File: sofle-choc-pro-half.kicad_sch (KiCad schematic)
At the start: 194 parts, among them J1 Connector, USB-TYPE-C-16P, J2 Connector, USB-TYPE-C-16P, J3 OLED 128x32, SW1 BOOT, SW10 F0, SW11 F1, SW12 F2, SW13 F3, SW14 F4, SW15 F5, SW16 F6 Choc/EC11, SW2 RESET, SW20 N0, SW21 N1, SW22 N2, SW23 N3, SW24 N4, SW25 N5, SW30 T0, SW31 T1, SW32 T2, SW33 T3, SW34 T4, SW35 T5, SW40 H0, SW41 H1, SW42 H2, SW43 H3, SW44 H4, SW45 H5, SW50 B0, SW51 B1, SW52 B2, SW53 B3, SW54 B4, SW55 B5, SW60 TH0, SW61 TH1, SW62 TH2, SW63 TH3, SW64 TH4, SW65 TH5 Choc/EC11, U1 RP2040, U2 USBLC6-2P6, U3 W25Q128JVPIQ, U4 USBLC6-2P6, U5 AP2112K-3.3, U6 SN74LV1T34DBVR, X1 ABM8-272-T3

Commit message: feat(pcb): put both halves in one project and one board
Both halves now live in one KiCad project: the schematic is one half sheet
used twice, as sheets Left and Right, and one board carries both halves
10 mm apart, so they are seen, checked and ordered together. Nothing moved
or was rewired: every pad sits where it did on the two old boards and every
pad net matches the new schematic.

- Edit sofle-choc-pro-half.kicad_sch once and both halves follow; Right
  references are the Left ones + 200
- Every net is per half, power included, through local power symbols, so
  the two halves can never join into one net
- One Ergogen run builds both halves, and the USB-C notches, case ports,
  spacer pockets and display openings hang off J1-J3 points, so board and
  case cannot drift apart
- Placement, LED snapping and hole placement work on both halves by
  (half, role)

Under the hood:
- sch: global labels made local; VBUS_FUSED names the F1-D1 net, which
  only had an auto name; H1-H5 are MountingHole symbols now
- pcb: right board brought in +139 mm with fresh UUIDs; its 29 unplaced
  support parts parked below it; pours clipped at the midline; J1/J2
  origins moved onto the board edge; the right HOST/LINK labels mirrored
  from the left, since they were stale copies at the left's coordinates
- rules: net class patterns and pair rules use sheet-prefixed names, which
  bare names never match; one skew rule per half so the pairs are not
  compared across halves
- ergogen: make_right.js becomes make_both.js; mounts.json replaces
  screws.json
- scripts: halves.py added; place_mounting_holes.py folded into
  place_from_ergogen.py; strip_signals.py keeps VBUS_FUSED as power
- fixes: the holes and J1/J2 had bare footprint ids or no sheet fields

ERC 0, parity 0, 452 unconnected (194 + 258, unrouted). DRC errors are the
26 known hole courtyard overlaps, 13 per half.
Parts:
- added H1, H2, H3, H4, H5: MountingHole, MountingHole:MountingHole_2.2mm_M2, symbol Mechanical:MountingHole
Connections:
- net VBUS_FUSED: now reaches D1.2, F1.2
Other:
- note added: "MOUNTING HOLES (placed from ergogen screw points)"

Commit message: feat(pcb): add a vbus tvs to both halves and move r210's via off its pad
Raw VBUS at each USB-C port now has surge protection ahead of the fuse,
and the right half's VBUS sense via no longer sits in a pad.

- D2/D202: SMF5.0A (LCSC C19077497, SOD-123FL) from VBUS to GND in the
  half sheet, on B.Cu beside J1/J201 with a 0.5 mm stub to the VBUS via
- D202 sits 1 mm east of the tightest spot so the B pour still feeds
  the right J1 GND patch (closer, the patch became isolated copper)
- The USB-C HOST labels move 2.7 mm down, clear of the new diodes
- R210's VBUS via moves beside pad 1 (it was centred in it and
  untented), fed on F.Cu past F201's VBUS_FUSED via

Verified: ERC 0 errors (27 warnings, unchanged); DRC 26
courtyards_overlap, 0 unconnected, 0 parity at all severities; GND
connected on both halves; jumper pad groups intact.
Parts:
- added D2: SMF5.0A, PCM_JLCPCB:D_SOD-123FL, symbol PCM_JLCPCB-Diodes:TVS-Uni,SMF5.0A
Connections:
- net GND: now also D2.2
- net VBUS: now also D2.1

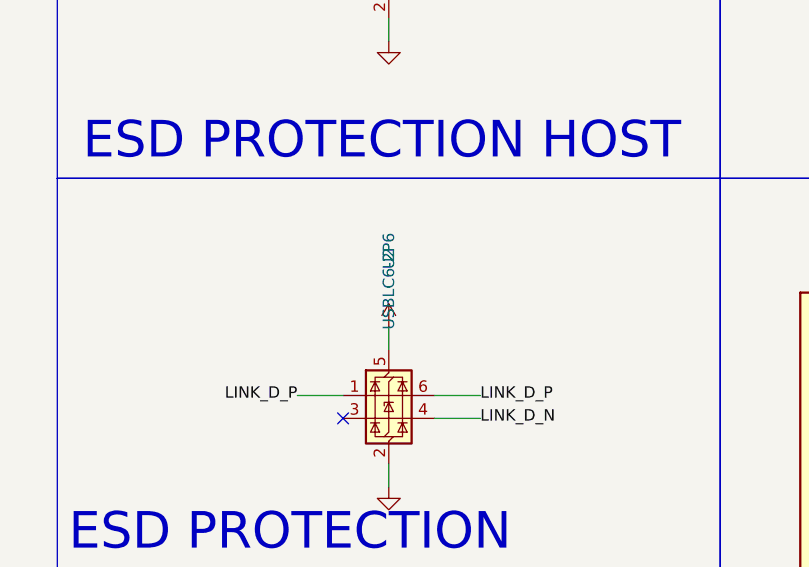
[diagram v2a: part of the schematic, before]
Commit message: fix(sch): give the 12 mhz crystal its own abm8-272-t3 symbol
X1/X201 borrowed the JLCPCB library's 20 pF crystal symbol (a different
part, C9002), so reviews flagged a 20 pF crystal on 15 pF load caps.

- New my-soffle:ABM8-272-T3_C20625731 symbol: same graphic and
  footprint, fields from the Abracon datasheet (10 pF load, C20625731)
- Frequency stability and 25 C tolerance corrected to +/-30 ppm (were
  the borrowed part's +/-20 and +/-10 ppm), on the board copies too
- Blank stock/price fields dropped from the new symbol

Verified: ERC 0 errors (27 warnings, unchanged); DRC 26
courtyards_overlap, 0 unconnected, 0 parity at all severities.
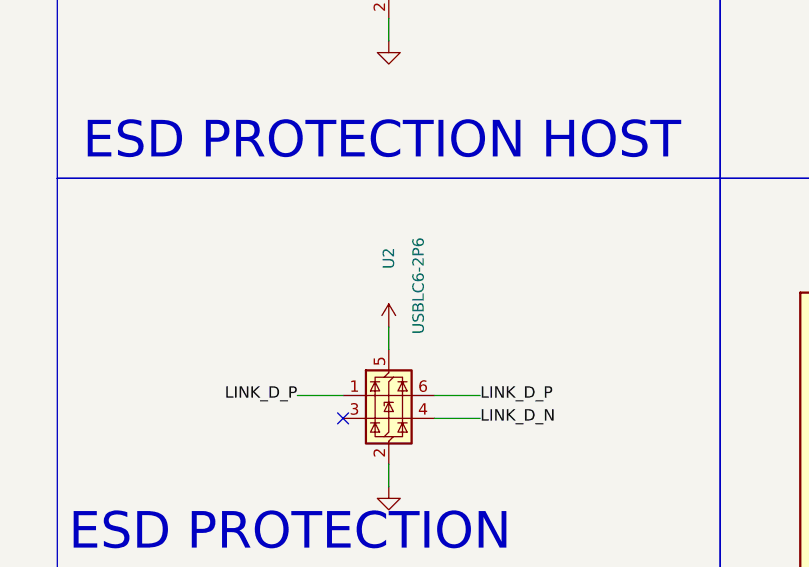
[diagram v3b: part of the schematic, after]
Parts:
- X1: symbol PCM_JLCPCB-Crystals:Crystal, 12MHz, 20pF -> my-soffle:ABM8-272-T3_C20625731; Frequency Stability ±20ppm -> ±30ppm; Normal Temperature Frequency Tolerance ±10ppm -> ±30ppm

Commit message: build(lib): vendor the used jlcpcb parts so the project opens anywhere
A clean clone now opens with every symbol, footprint and 3D model in
place: no Plugin and Content Manager package or KICAD8_3RD_PARTY path
is needed. Without the library, a reviewer saw 244 ERC and 286 DRC
items (missing symbols and footprints) and 292 missing 3D models.

- lib/jlcpcb/: the 16 symbols, 8 footprints and 8 models the design
  uses, from CDFER/JLCPCB-Kicad-Library (MIT, LICENSE included)
- The Choc hotswap model (kiswitch) moves into lib/my-soffle.3dshapes
- sym-lib-table/fp-lib-table keep their nicknames with ${KIPRJMOD}
  paths; the unused Crystals and Diode-Packages entries are dropped
- R7/R8 (27 ohm, C25100) get their own my-soffle:0402_27R_C25100
  symbol instead of the library's 33 ohm one
- README says what to install for each task; rule file notes the
  vendored copy

Verified with KICAD8_3RD_PARTY pointing at an empty folder and without:
both give ERC 0 errors (27 warnings) and DRC 26 courtyards_overlap,
0 unconnected, 0 parity at all severities; every board model resolves.
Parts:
- R7, R8: symbol PCM_JLCPCB-Resistors:0402,33Ω -> my-soffle:0402_27R_C25100
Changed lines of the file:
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@@
 	)
 	(symbol
-		(lib_id "PCM_JLCPCB-Resistors:0402,33Ω")
+		(lib_id "my-soffle:0402_27R_C25100")
 		(at 140.97 91.44 180)
 		(unit 1)
@@
 			)
 		)
-		(property "Description" ""
+		(property "Description" "27Ω ±1% 62.5mW 0402 thick film resistor (USB series termination)"
 			(at 140.97 91.44 0)
 			(hide yes)
@@
 	)
 	(symbol
-		(lib_id "PCM_JLCPCB-Resistors:0402,33Ω")
+		(lib_id "my-soffle:0402_27R_C25100")
 		(at 143.51 91.44 180)
 		(unit 1)
@@
 			)
 		)
-		(property "Description" ""
+		(property "Description" "27Ω ±1% 62.5mW 0402 thick film resistor (USB series termination)"
 			(at 143.51 91.44 0)
 			(hide yes)

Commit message: fix(pcb): place the usb-c connectors on jlc's footprint origin
The four USB-C receptacles were told to sit 2.55 mm from where their
pads are, so an assembled board would have had every host and link
connector misplaced. The offset that positions them was measured for
the old connector and never revisited when the board moved to the
mid-mount part.

- J1, J2, J201 and J202 now land on the pad field, matching JLC's own
  footprint for C19274022 to within 0.07 mm
- FT Position Offset goes from 0,1.394 to 0,3.945, the distance from
  our footprint's anchor at the connector mouth to that pad field
- README and the KiCad rules record why the Fabrication Toolkit runs
  with automatic translation off, and that a part swap invalidates a
  part's offset

Derived by fitting JLC's own footprints onto ours, the method that
reproduces the three offsets already on the board (270 on the SOT-563
and WSON-8, 180 on the stock SOT-23-5). ERC 0 errors; DRC 42 known
items, 0 unconnected, 0 parity.
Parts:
- J1, J2: FT Position Offset 0,1.394 -> 0,3.945
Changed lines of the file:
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@@
 			)
 		)
-		(property "FT Position Offset" "0,1.394"
+		(property "FT Position Offset" "0,3.945"
 			(at 29.21 39.37 0)
 			(hide yes)
@@
 			)
 		)
-		(property "FT Position Offset" "0,1.394"
+		(property "FT Position Offset" "0,3.945"
 			(at 109.22 271.78 0)
 			(hide yes)

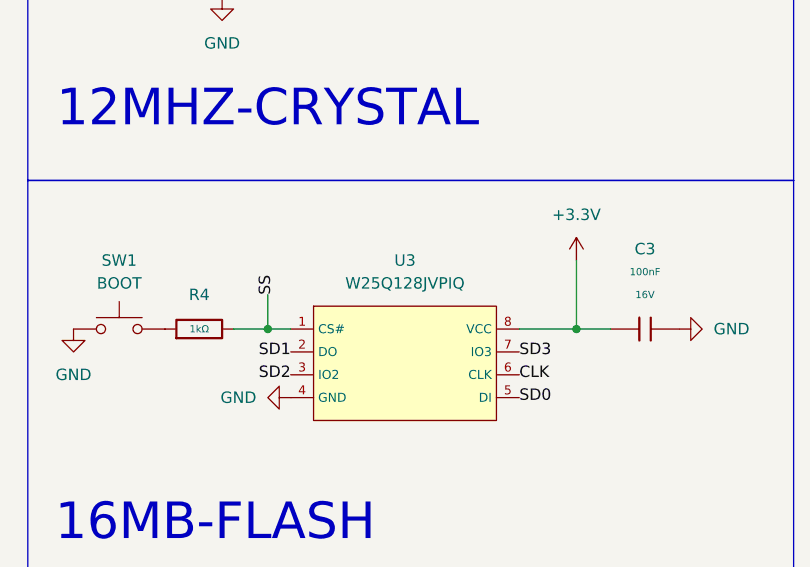
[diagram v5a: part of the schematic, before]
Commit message: feat(sch): swap the flash to the zetta zd25q128c
The Winbond W25Q128JVPIQ had climbed to EUR 2.74 each and fallen to
385 in stock at JLCPCB, making it both the most expensive line on the
board and the one most likely to be unavailable at order time. The
Zetta part is the same 128 Mbit in the same package for a third of the
money, so capacity is unchanged.

- EUR 27.39 to EUR 8.47 for the ten pieces a 5 board run needs, and
  2193 in stock instead of 385
- No copper changes: pin for pin identical (1 CS#, 2 SO/IO1, 3 WP#/IO2,
  4 VSS, 5 SI/IO0, 6 SCLK, 7 HOLD#/IO3, 8 VCC) on the same WSON-8 6x5
  land, verified against the part's own datasheet table 1 and against
  the RP2040 QSPI pins in its table 616
- FT Rotation Offset drops from 270 to 0, because JLC's drawing for
  this part sits 90 degrees from the Winbond one; U3 now writes 0 and
  U203 writes 90 into the placement file
- datasheets/ tracks the new part and drops the superseded one, and
  picks up the SMF5.0A sheet that was missing

ERC 0 errors; DRC 42 known items, 0 unconnected, 0 parity.
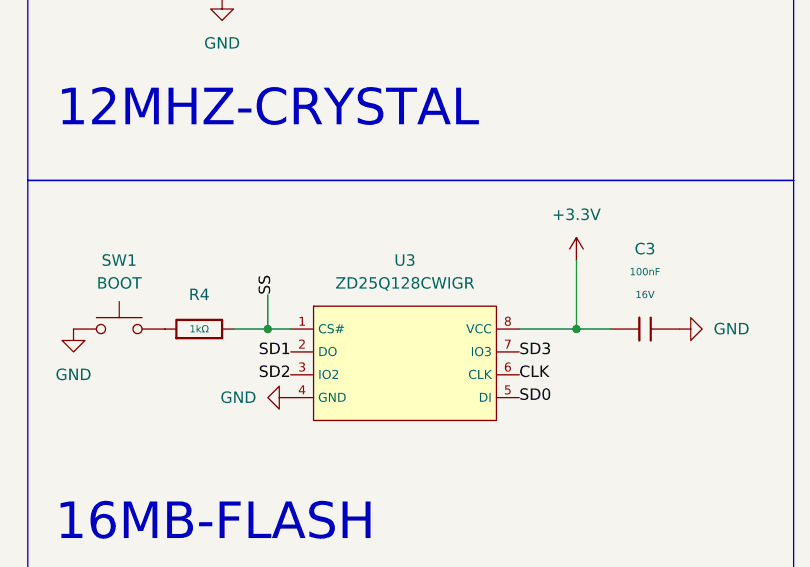
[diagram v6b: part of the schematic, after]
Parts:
- U3: value W25Q128JVPIQ -> ZD25Q128CWIGR; Class Basic Component -> Extended Component; FT Rotation Offset 270 -> 0; LCSC C190862 -> C53959302; Manufacturer Winbond Elec -> Zetta; Part W25Q128JVPIQ -> ZD25Q128CWIGR; Price 0.896USD -> 0.9687USD; Stock 80440 -> 2193
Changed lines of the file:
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@@
 			)
 		)
-		(property "Value" "W25Q128JVPIQ"
+		(property "Value" "ZD25Q128CWIGR"
 			(at 55.88 161.29 0)
 			(show_name no)
@@
 			)
 		)
-		(property "Datasheet" "https://www.lcsc.com/datasheet/lcsc_datasheet_1811151432_Winbond-Elec-W25Q128JVPIQ_C190862.pdf"
+		(property "Datasheet" "https://www.lcsc.com/datasheet/C53959302.pdf"
 			(at 53.594 171.323 0)
 			(hide yes)
@@
 			)
 		)
-		(property "Description" "128Mbit SOIC-8-208mil NOR FLASH ROHS"
+		(property "Description" "128Mbit WSON-8-EP(6x5) NOR FLASH ROHS"
 			(at 55.88 171.45 0)
 			(hide yes)
@@
 			)
 		)
-		(property "LCSC" "C190862"
+		(property "LCSC" "C53959302"
 			(at 55.88 171.45 0)
 			(hide yes)
@@
 			)
 		)
-		(property "FT Rotation Offset" "270"
+		(property "FT Rotation Offset" "0"
 			(at 55.88 171.45 0)
 			(hide yes)
@@
 			)
 		)
-		(property "Stock" "80440"
+		(property "Stock" "2193"
 			(at 55.88 171.45 0)
 			(hide yes)
@@
 			)
 		)
-		(property "Price" "0.896USD"
+		(property "Price" "0.9687USD"
 			(at 55.88 171.45 0)
 			(hide yes)
@@
 			)
 		)
-		(property "Class" "Basic Component"
+		(property "Class" "Extended Component"
 			(at 55.88 171.45 0)
 			(hide yes)
@@
 			)
 		)
-		(property "Manufacturer" "Winbond Elec"
+		(property "Manufacturer" "Zetta"
 			(at 55.88 171.45 0)
 			(hide yes)
@@
 			)
 		)
-		(property "Part" "W25Q128JVPIQ"
+		(property "Part" "ZD25Q128CWIGR"
 			(at 55.88 171.45 0)
 			(hide yes)
